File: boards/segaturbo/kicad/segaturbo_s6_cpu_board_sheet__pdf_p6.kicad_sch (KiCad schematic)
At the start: 17 parts, among them CN7 Conn_01x26, IC123 8255, IC18 74LS157, IC19 74LS157, IC31 74LS157, IC32 8255, IC55 74LS86, IC56 74LS283, IC57 74LS283, IC58 74LS283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

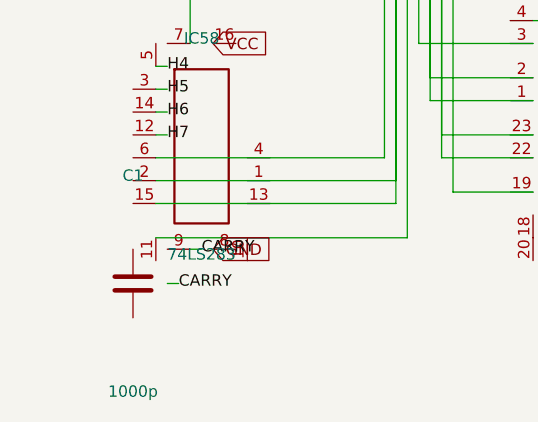
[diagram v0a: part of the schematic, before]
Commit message: Fix KiCad pin-aligned generated symbols
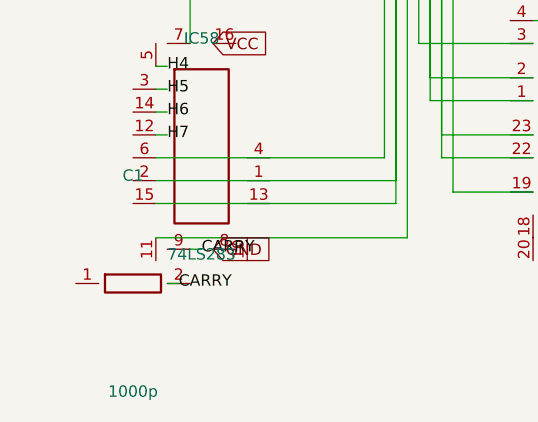
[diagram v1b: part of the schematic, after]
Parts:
- C1: symbol Device:C -> user:_chip_C1
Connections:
- net CARRY: now also C1.2
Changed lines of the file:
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@@
   )
   (symbol
-    (lib_id "Device:C")
+    (lib_id "user:_chip_C1")
     (at 80.01 242.57 0)
     (unit 1)
